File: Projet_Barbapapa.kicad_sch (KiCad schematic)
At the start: 3 parts, among them J6 Random FTDI, J9 RGB_LED

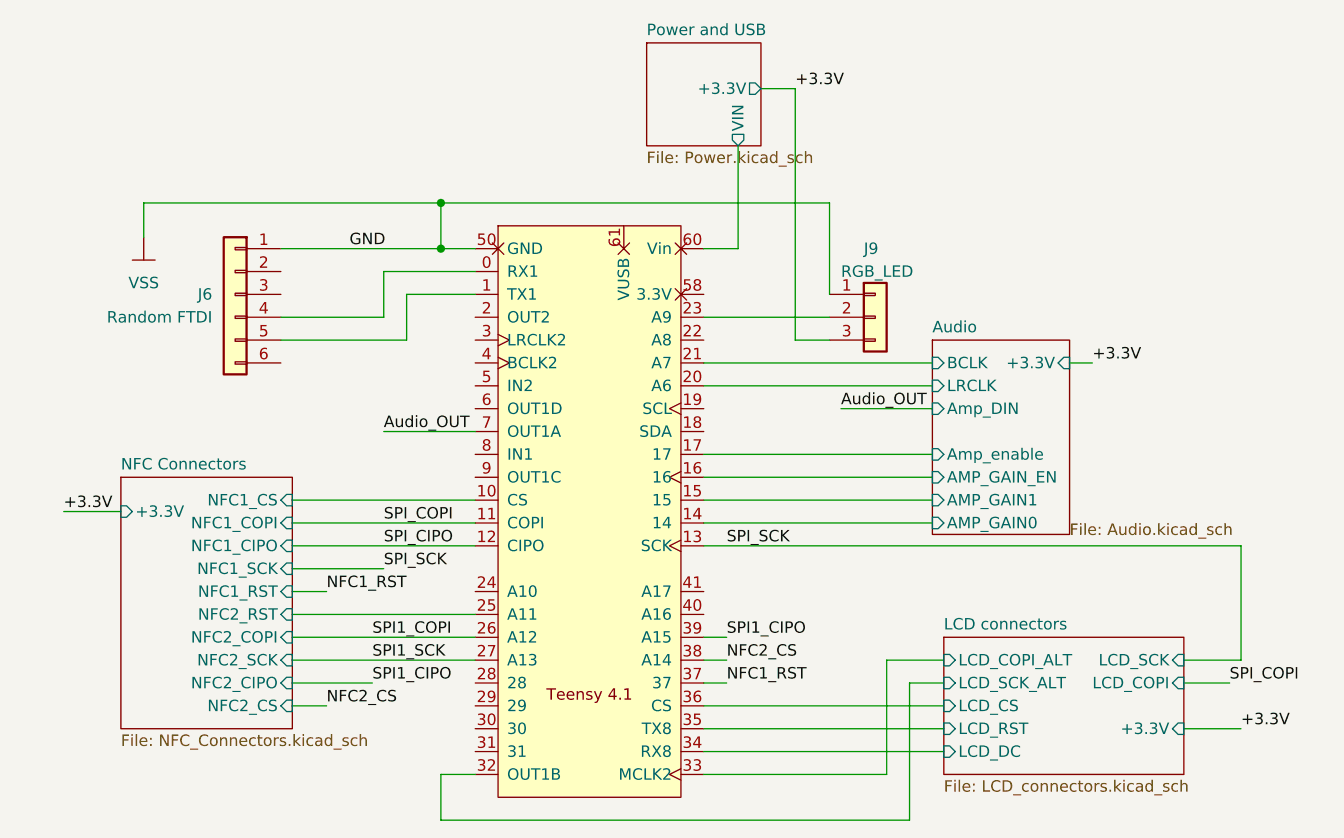
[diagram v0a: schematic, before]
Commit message: Améliorations après retour Victor
Allumage du régulateur maintenant géré par la teensy
Compaction de la carte pour rentrer sur 100x100mm
Ajout des trous de montage
Routage de la puissance du port USB maintenant sans boucle !
Un peu plus d'espace pour l'ampli'
Routage de l'ampli' avec des plans sur la sortie et une via par
condo pour l'entrée.
Moins de vias thermiques
Un seule via dans le pad de l'ampli'
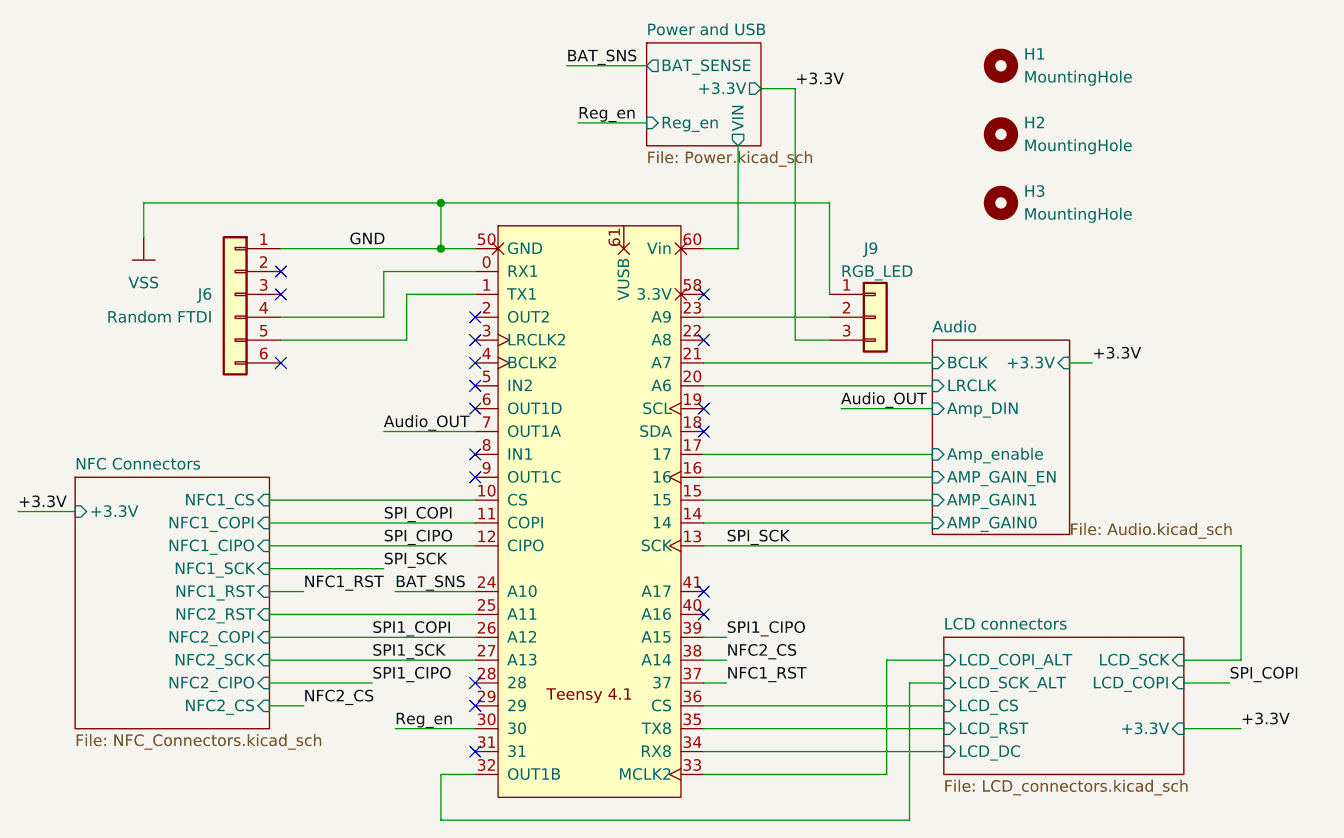
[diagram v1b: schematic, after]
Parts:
- added H1, H2, H3: MountingHole, MountingHole:MountingHole_3.2mm_M3, symbol Mechanical:MountingHole
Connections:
- net BAT_SNS: now reaches T4_1.24 (A10)
- net Reg_en: now reaches T4_1.30
- no-connect marks 0 -> 19
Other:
- sheet Power and USB ports: added BAT_SENSE, Reg_en; removed none

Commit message: Rev 0.3: Passage sur deux couches
Passage sur deux couches, ajustement de l'impédance pour l'USB.
Reroutage de l'alimentation côté USB
Ajout de beaucoup de silk
Quelques ajustements de nets pour la lisbilité
Ajout de LEDs de debug
Plan de masse sur le top
Quelques mises à jour sur le schematic
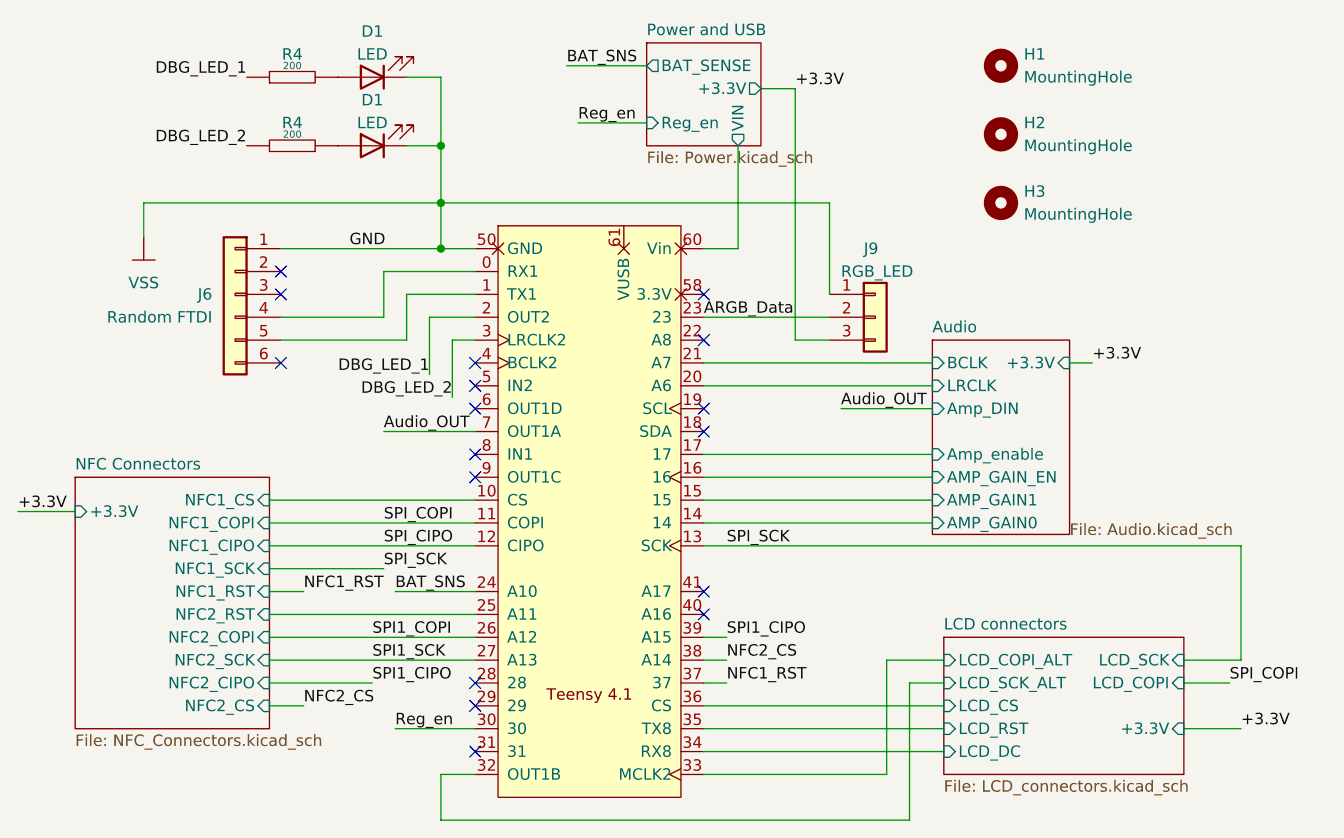
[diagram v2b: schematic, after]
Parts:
- added D1 (x2): LED, LED_SMD:LED_0603_1608Metric_Pad1.05x0.95mm_HandSolder, symbol Device:LED
- added R4 (x2): RES_0603_200_1%, 01_Passives:RES_0603, symbol 02_Resistor:RES_0603_2K1_1%
- H1, H2, H3, J6, J9: now left out of the parts list
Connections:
- net GND: now also D1.1 (K), D1.1 (K)
- net DBG_LED_1: now reaches T4_1.2 (OUT2)
- net DBG_LED_1: now also R4.1
- net ARGB_Data: now reaches J9.2 (Pin_2), T4_1.23 (A9)
- net DBG_LED_2: now reaches T4_1.3 (LRCLK2)
- net DBG_LED_2: now also R4.2
- new net: D1.2 (A), R4.2
- new net: D1.2 (A), R4.1
- no-connect marks 19 -> 17
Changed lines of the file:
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@@
   (title_block
     (title "Projet Barbapapa")
-    (date "2023-06-22")
-    (rev "0.2")
+    (date "2023-06-25")
+    (rev "0.3")
     (company "Téo-CD")
   )
@@
   (junction (at 86.36 85.09) (diameter 0) (color 0 0 0 0)
   )
-  (no_connect (at 90.17 97.79))
+  (junction (at 86.36 78.74) (diameter 0) (color 0 0 0 0)
+  )
   (no_connect (at 90.17 140.97))
   (no_connect (at 115.57 107.95))
@@
   (no_connect (at 90.17 115.57))
   (no_connect (at 90.17 105.41))
-  (no_connect (at 90.17 100.33))
   (no_connect (at 68.58 95.25))
   (no_connect (at 90.17 102.87))
@@
     (stroke (width 0) (type default))
   )
+  (wire (pts (xy 85.09 97.79) (xy 90.17 97.79))
+    (stroke (width 0) (type default))
+  )
+  (wire (pts (xy 86.36 71.12) (xy 86.36 78.74))
+    (stroke (width 0) (type default))
+  )
   (wire (pts (xy 119.38 78.74) (xy 119.38 90.17))
     (stroke (width 0) (type default))
@@
     (stroke (width 0) (type default))
   )
+  (wire (pts (xy 90.17 100.33) (xy 87.63 100.33))
+    (stroke (width 0) (type default))
+  )
   (wire (pts (xy 135.89 148.59) (xy 135.89 135.89))
     (stroke (width 0) (type default))
@@
     (stroke (width 0) (type default))
   )
+  (wire (pts (xy 85.09 104.14) (xy 85.09 97.79))
+    (stroke (width 0) (type default))
+  )
   (wire (pts (xy 115.57 120.65) (xy 140.97 120.65))
     (stroke (width 0) (type default))
@@
     (stroke (width 0) (type default))
   )
+  (wire (pts (xy 87.63 100.33) (xy 87.63 106.68))
+    (stroke (width 0) (type default))
+  )
   (wire (pts (xy 115.57 140.97) (xy 142.24 140.97))
     (stroke (width 0) (type default))
@@
     (stroke (width 0) (type default))
   )
+  (wire (pts (xy 86.36 78.74) (xy 86.36 85.09))
+    (stroke (width 0) (type default))
+  )
   (wire (pts (xy 115.57 102.87) (xy 140.97 102.87))
     (stroke (width 0) (type default))
@@
     (stroke (width 0) (type default))
   )
+  (wire (pts (xy 82.55 78.74) (xy 86.36 78.74))
+    (stroke (width 0) (type default))
+  )
   (wire (pts (xy 118.11 135.89) (xy 115.57 135.89))
     (stroke (width 0) (type default))
@@
     (stroke (width 0) (type default))
   )
+  (wire (pts (xy 82.55 71.12) (xy 86.36 71.12))
+    (stroke (width 0) (type default))
+  )
   (wire (pts (xy 53.34 85.09) (xy 86.36 85.09))
     (stroke (width 0) (type default))
@@
     (effects (font (size 1.27 1.27)) (justify left bottom))
   )
+  (label "ARGB_Data" (at 115.57 97.79 0) (fields_autoplaced)
+    (effects (font (size 1.27 1.27)) (justify left bottom))
+  )
   (label "SPI1_COPI" (at 78.74 133.35 0) (fields_autoplaced)
     (effects (font (size 1.27 1.27)) (justify left bottom))
   )
+  (label "DBG_LED_1" (at 85.09 104.14 180) (fields_autoplaced)
+    (effects (font (size 1.27 1.27)) (justify right bottom))
+  )
   (label "Reg_en" (at 81.28 143.51 0) (fields_autoplaced)
     (effects (font (size 1.27 1.27)) (justify left bottom))
   )
+  (label "DBG_LED_1" (at 64.77 71.12 180) (fields_autoplaced)
+    (effects (font (size 1.27 1.27)) (justify right bottom))
+  )
   (label "NFC2_CS" (at 118.11 135.89 0) (fields_autoplaced)
     (effects (font (size 1.27 1.27)) (justify left bottom))
@@
     (effects (font (size 1.27 1.27)) (justify left bottom))
   )
+  (label "DBG_LED_2" (at 87.63 106.68 180) (fields_autoplaced)
+    (effects (font (size 1.27 1.27)) (justify right bottom))
+  )
+  (label "DBG_LED_2" (at 64.77 78.74 180) (fields_autoplaced)
+    (effects (font (size 1.27 1.27)) (justify right bottom))
+  )
   (label "SPI_COPI" (at 173.99 138.43 0) (fields_autoplaced)
     (effects (font (size 1.27 1.27)) (justify left bottom))
@@
   (label "NFC2_CS" (at 71.12 140.97 0) (fields_autoplaced)
     (effects (font (size 1.27 1.27)) (justify left bottom))
+  )
+  (symbol (lib_id "02_Resistor:RES_0603_2K1_1%") (at 69.85 71.12 0) (mirror x) (unit 1)
+    (in_bom yes) (on_board yes) (dnp no)
+    (property "Reference" "R4" (at 69.85 68.58 0)
+      (effects (font (size 1.27 1.27)))
+    )
+    (property "Value" "RES_0603_200_1%" (at 73.66 78.74 0)
+      (effects (font (size 1.27 1.27)) hide)
+    )
+    (property "Footprint" "01_Passives:RES_0603" (at 69.85 81.28 0)
+      (effects (font (size 1.27 1.27)) hide)
+    )
+    (property "Datasheet" "" (at 69.85 71.12 0)
+      (effects (font (size 1.27 1.27)) hide)
+    )
+    (property "Resistance" "200" (at 69.85 69.85 0)
+      (effects (font (size 0.8 0.8)))
+    )
+    (property "Power" "100mW" (at 69.85 76.2 0)
+      (effects (font (size 1.27 1.27)) hide)
+    )
+    (pin "1")
+    (pin "2")
+    (instances
+      (project "Projet_Barbapapa"
+        (path "/1f7900b2-90c4-494b-ac10-3ced4db03c46/1ff48b82-bd33-4a97-91b8-e56f2808ae9f"
+          (reference "R4") (unit 1)
+        )
+        (path "/1f7900b2-90c4-494b-ac10-3ced4db03c46"
+          (reference "R13") (unit 1)
+        )
+      )
+    )
   )
   (symbol (lib_id "00_PowerSymboles:VSS") (at 53.34 88.9 0) (unit 1)
@@
   )
   (symbol (lib_id "Mechanical:MountingHole") (at 148.59 69.85 0) (unit 1)
-    (in_bom yes) (on_board yes) (dnp no) (fields_autoplaced)
+    (in_bom no) (on_board yes) (dnp no) (fields_autoplaced)
     (property "Reference" "H1" (at 151.13 68.58 0)
       (effects (font (size 1.27 1.27)) (justify left))
@@
     (pin "21")
     (pin "22")
-    (pin "23")
+    (pin "23" (alternate "23"))
     (pin "24")
     (pin "25")
@@
     )
   )
+  (symbol (lib_id "Device:LED") (at 78.74 78.74 180) (unit 1)
+    (in_bom yes) (on_board yes) (dnp no)
+    (property "Reference" "D1" (at 78.74 73.66 0)
+      (effects (font (size 1.27 1.27)))
+    )
+    (property "Value" "LED" (at 78.74 76.2 0)
+      (effects (font (size 1.27 1.27)))
+    )
+    (property "Footprint" "LED_SMD:LED_0603_1608Metric_Pad1.05x0.95mm_HandSolder" (at 78.74 78.74 0)
+      (effects (font (size 1.27 1.27)) hide)
+    )
+    (property "Datasheet" "~" (at 78.74 78.74 0)
+      (effects (font (size 1.27 1.27)) hide)
+    )
+    (pin "1")
+    (pin "2")
+    (instances
+      (project "Projet_Barbapapa"
+        (path "/1f7900b2-90c4-494b-ac10-3ced4db03c46/1ff48b82-bd33-4a97-91b8-e56f2808ae9f"
+          (reference "D1") (unit 1)
+        )
+        (path "/1f7900b2-90c4-494b-ac10-3ced4db03c46"
+          (reference "D4") (unit 1)
+        )
+      )
+    )
+  )
+  (symbol (lib_id "Device:LED") (at 78.74 71.12 180) (unit 1)
+    (in_bom yes) (on_board yes) (dnp no)
+    (property "Reference" "D1" (at 78.74 66.04 0)
+      (effects (font (size 1.27 1.27)))
+    )
+    (property "Value" "LED" (at 78.74 68.58 0)
+      (effects (font (size 1.27 1.27)))
+    )
+    (property "Footprint" "LED_SMD:LED_0603_1608Metric_Pad1.05x0.95mm_HandSolder" (at 78.74 71.12 0)
+      (effects (font (size 1.27 1.27)) hide)
+    )
+    (property "Datasheet" "~" (at 78.74 71.12 0)
+      (effects (font (size 1.27 1.27)) hide)
+    )
+    (pin "1")
+    (pin "2")
+    (instances
+      (project "Projet_Barbapapa"
+        (path "/1f7900b2-90c4-494b-ac10-3ced4db03c46/1ff48b82-bd33-4a97-91b8-e56f2808ae9f"
+          (reference "D1") (unit 1)
+        )
+        (path "/1f7900b2-90c4-494b-ac10-3ced4db03c46"
+          (reference "D3") (unit 1)
+        )
+      )
+    )
+  )
   (symbol (lib_id "Mechanical:MountingHole") (at 148.59 85.09 0) (unit 1)
-    (in_bom yes) (on_board yes) (dnp no) (fields_autoplaced)
+    (in_bom no) (on_board yes) (dnp no) (fields_autoplaced)
     (property "Reference" "H3" (at 151.13 83.82 0)
       (effects (font (size 1.27 1.27)) (justify left))
@@
     )
   )
+  (symbol (lib_id "02_Resistor:RES_0603_2K1_1%") (at 69.85 78.74 180) (unit 1)
+    (in_bom yes) (on_board yes) (dnp no)
+    (property "Reference" "R4" (at 69.85 76.2 0)
+      (effects (font (size 1.27 1.27)))
+    )
+    (property "Value" "RES_0603_200_1%" (at 66.04 86.36 0)
+      (effects (font (size 1.27 1.27)) hide)
+    )
+    (property "Footprint" "01_Passives:RES_0603" (at 69.85 88.9 0)
+      (effects (font (size 1.27 1.27)) hide)
+    )
+    (property "Datasheet" "" (at 69.85 78.74 0)
+      (effects (font (size 1.27 1.27)) hide)
+    )
+    (property "Resistance" "200" (at 69.85 77.47 0)
+      (effects (font (size 0.8 0.8)))
+    )
+    (property "Power" "100mW" (at 69.85 83.82 0)
+      (effects (font (size 1.27 1.27)) hide)
+    )
+    (pin "1")
+    (pin "2")
+    (instances
+      (project "Projet_Barbapapa"
+        (path "/1f7900b2-90c4-494b-ac10-3ced4db03c46/1ff48b82-bd33-4a97-91b8-e56f2808ae9f"
+          (reference "R4") (unit 1)
+        )
+        (path "/1f7900b2-90c4-494b-ac10-3ced4db03c46"
+          (reference "R14") (unit 1)
+        )
+      )
+    )
+  )
   (symbol (lib_id "Connector_Generic:Conn_01x06") (at 63.5 95.25 0) (mirror y) (unit 1)
-    (in_bom yes) (on_board yes) (dnp no)
+    (in_bom no) (on_board yes) (dnp no)
     (property "Reference" "J6" (at 60.96 95.25 0)
       (effects (font (size 1.27 1.27)) (justify left))
@@
   )
   (symbol (lib_id "Mechanical:MountingHole") (at 148.59 77.47 0) (unit 1)
-    (in_bom yes) (on_board yes) (dnp no) (fields_autoplaced)
+    (in_bom no) (on_board yes) (dnp no) (fields_autoplaced)
     (property "Reference" "H2" (at 151.13 76.2 0)
       (effects (font (size 1.27 1.27)) (justify left))
@@
   )
   (symbol (lib_id "Connector_Generic:Conn_01x03") (at 134.62 97.79 0) (unit 1)
-    (in_bom yes) (on_board yes) (dnp no)
+    (in_bom no) (on_board yes) (dnp no)
     (property "Reference" "J9" (at 133.35 90.17 0)
       (effects (font (size 1.27 1.27)) (justify left))
